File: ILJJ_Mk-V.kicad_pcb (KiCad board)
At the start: 2 copper layers, 48.3 x 99.1 mm, 12 parts, among them J1 Conn_02x12, U1 74LS00, U10 74LS00, U11 74LS00, U2 74LS00, U3 74LS00, U4 74LS00, U5 74LS00, U6 74LS00, U7 74LS00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

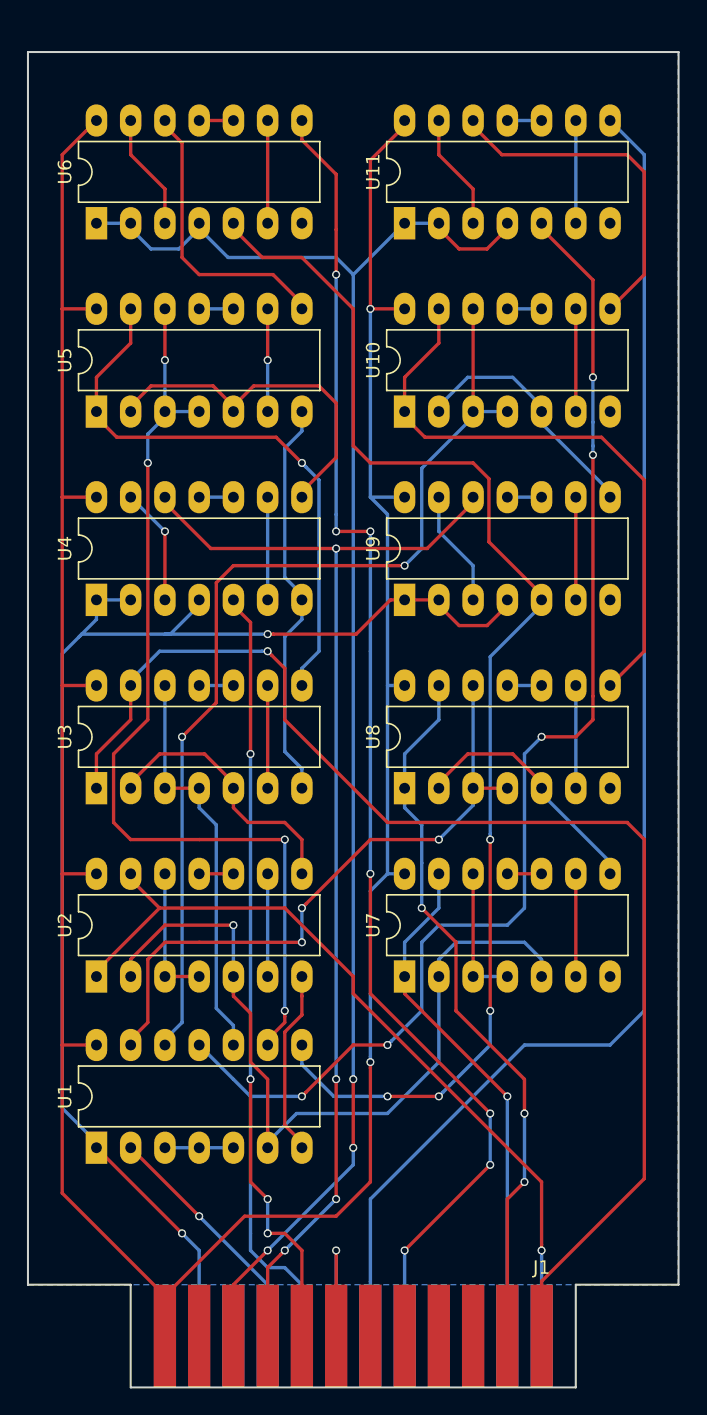
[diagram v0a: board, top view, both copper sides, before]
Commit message: [add] #2 ネジ穴を追加
パーツこれであってるのかわからんけどw
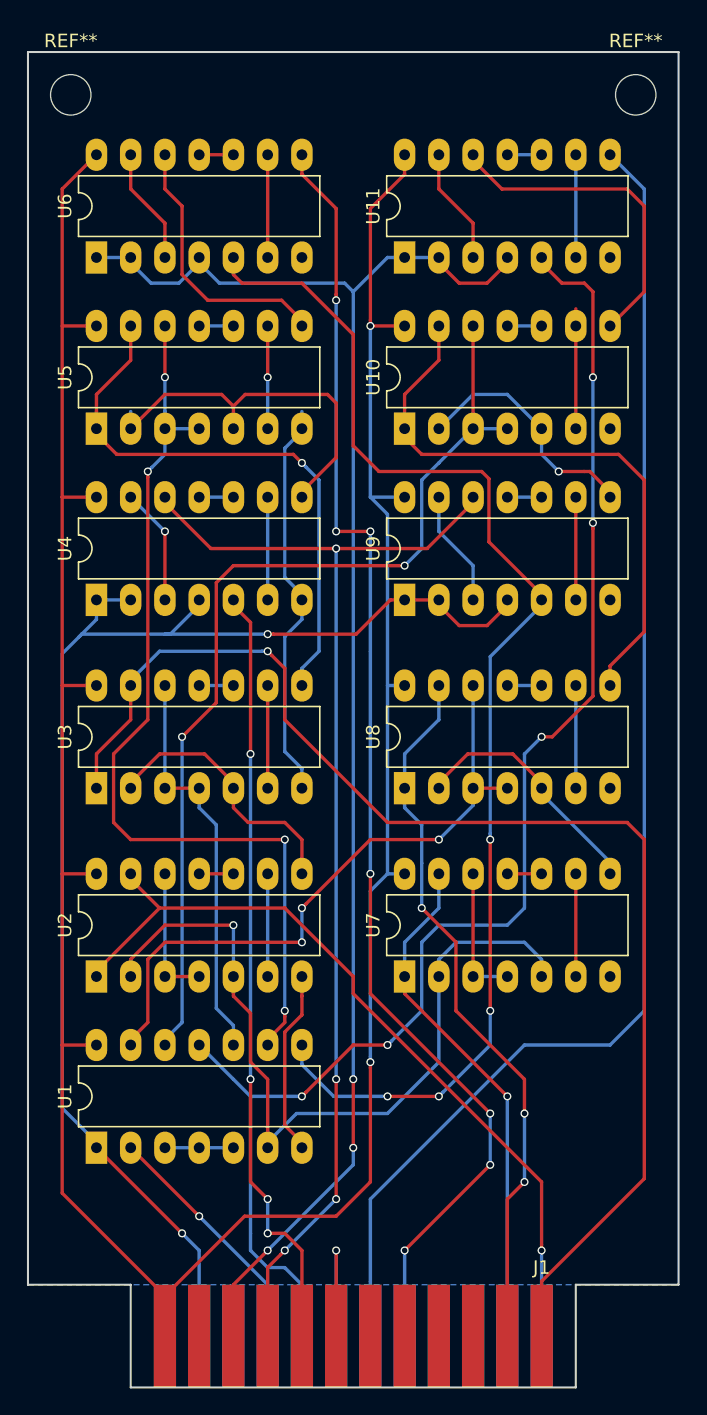
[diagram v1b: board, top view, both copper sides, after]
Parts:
- added REF**: MountingHole_3mm, Mounting_Holes:MountingHole_3mm, F.Cu at (104.8, 54.0)
- added REF**: MountingHole_3mm, Mounting_Holes:MountingHole_3mm, F.Cu at (146.7, 54.0)
- moved U11 2.54 mm to (129.5, 66.0)
- moved U6 2.54 mm to (106.7, 66.0)
- moved U10 1.27 mm to (129.5, 78.7)
- moved U5 1.27 mm to (106.7, 78.7)
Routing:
- net VCC: track 214.3 -> 209.2 mm
- net /S0: track 100.5 -> 97.5 mm
- net /Cout: track 110.6 -> 108.0 mm
- net /S1: track 103.4 -> 100.8 mm
- net /F1: track 120.0 -> 117.7 mm
- net /IBC: track 96.2 -> 94.5 mm
- net Net-(U1-Pad12): track 74.1 -> 72.8 mm
- net /FA1_S: track 25.7 -> 24.5 mm
- net /FA0_S: track 21.4 -> 20.1 mm
- net Net-(U10-Pad1): track 45.1 -> 44.1 mm
- net /FA1_Cin: track 19.0 -> 18.3 mm, vias 0 -> 1
- net /FA0_Cin: track 27.3 -> 26.5 mm
